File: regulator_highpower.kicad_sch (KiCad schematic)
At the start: 14 parts, among them U12 I3A4W008A033V-001-R, U13 INA180A2

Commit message: improvements with derick
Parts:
- D11: value BLUE -> GREEN
- R43: value Rup -> 8K2
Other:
- note added: "SMPS Regulator (1/32 Brick DC/DC)"
- note added: "Vref = 0.6V Vonom = 2.59V F = 36500 G = 511 Rext = (Vref * F) / (Vout - Vonom) - G Vout = 5.1V -> 8.214K Vout = 18V -> 910"
- note removed: "SMPS Regulator"
- note removed: "TODO: Rup TODO: DAC?"
- moved on the sheet: C27, C28, C29, R43, U12

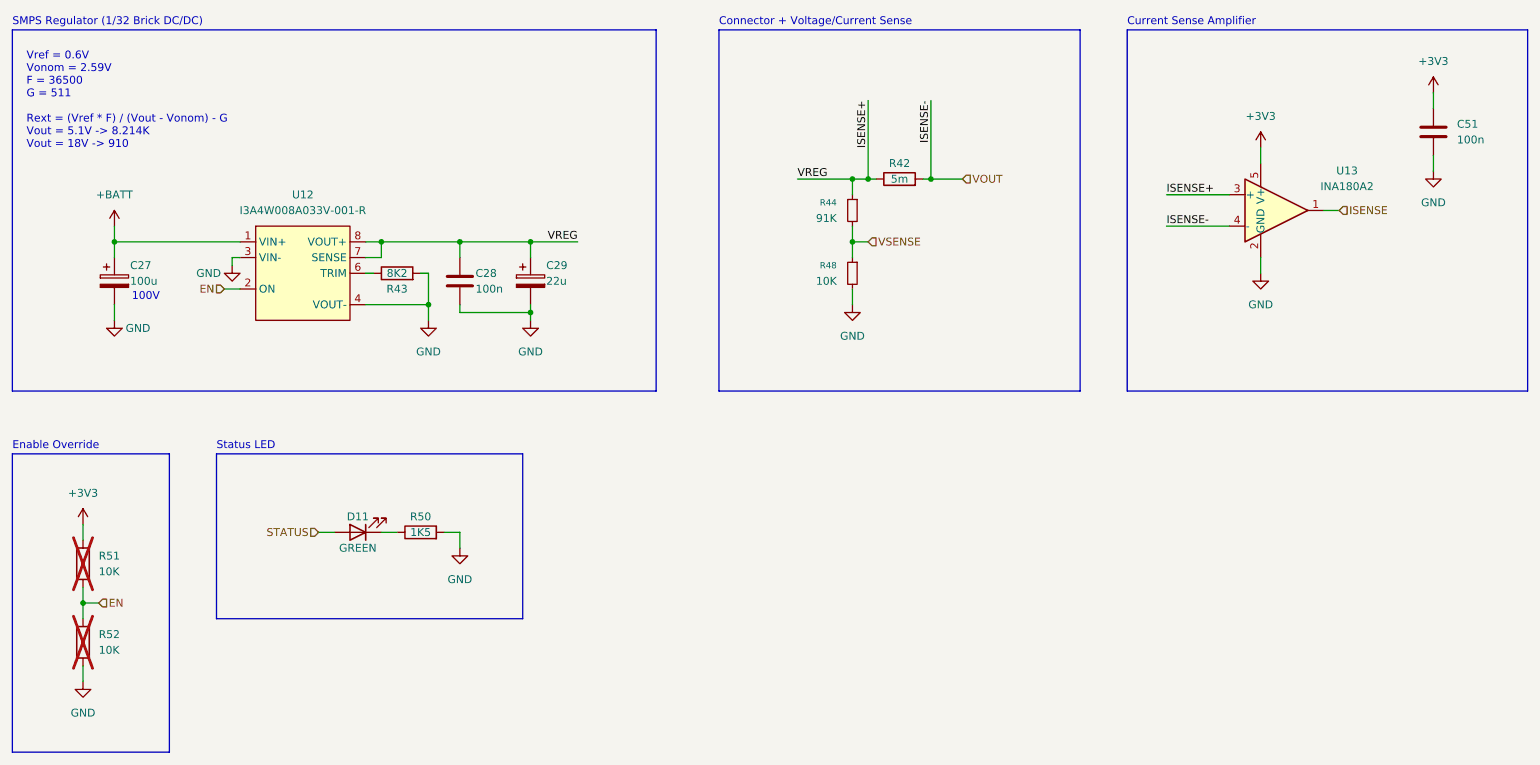
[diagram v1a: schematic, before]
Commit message: updated layout for fault led with new circuit, rerouted
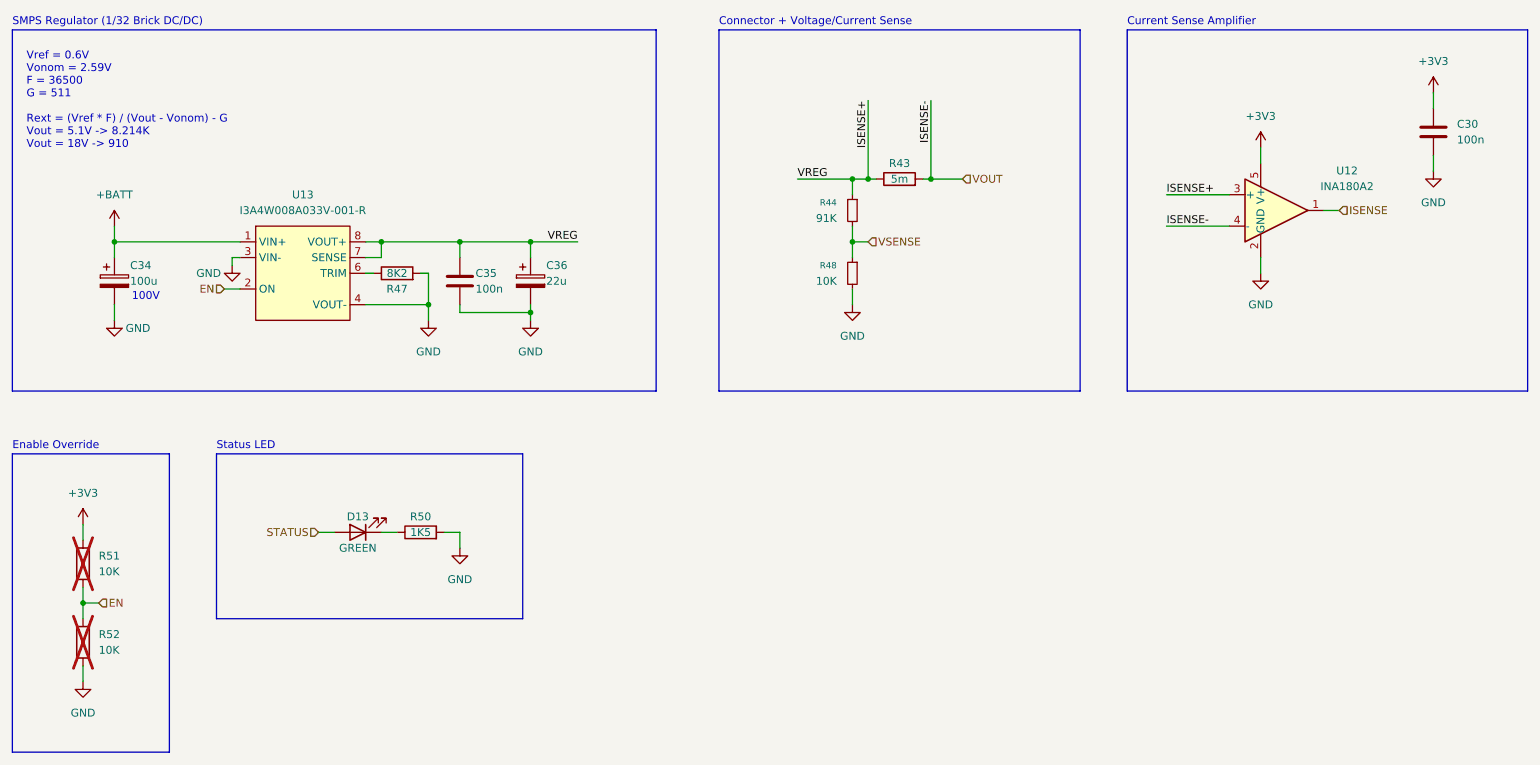
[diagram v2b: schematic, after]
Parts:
- renumbered C51 to C30, C27 to C34, C28 to C35, C29 to C36, D11 to D13, R42 to R43, R43 to R47, U13 to U12, U12 to U13
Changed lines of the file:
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@@
 		(dnp no)
 		(fields_autoplaced yes)
-		(property "Reference" "#PWR071"
+		(property "Reference" "#PWR0101"
 			(at 36.83 57.15 0)
 			(effects
@@
 			(project "vrb"
 				(path "/59a9b615-ea12-4a8c-9228-b32f861e8d75/eb1e4a76-3344-4a3b-8543-2ea356ffbe51"
-					(reference "#PWR071")
+					(reference "#PWR0101")
 					(unit 1)
 				)
@@
 		(dnp no)
 		(fields_autoplaced yes)
-		(property "Reference" "U12"
+		(property "Reference" "U13"
 			(at 67.31 48.26 0)
 			(effects
@@
 			(project "vrb"
 				(path "/59a9b615-ea12-4a8c-9228-b32f861e8d75/eb1e4a76-3344-4a3b-8543-2ea356ffbe51"
-					(reference "U12")
+					(reference "U13")
 					(unit 1)
 				)
@@
 		(on_board yes)
 		(dnp no)
-		(property "Reference" "C28"
+		(property "Reference" "C35"
 			(at 95.25 60.96 0)
 			(effects
@@
 			(project "vrb"
 				(path "/59a9b615-ea12-4a8c-9228-b32f861e8d75/eb1e4a76-3344-4a3b-8543-2ea356ffbe51"
-					(reference "C28")
+					(reference "C35")
 					(unit 1)
 				)
@@
 		(on_board yes)
 		(dnp no)
-		(property "Reference" "R42"
+		(property "Reference" "R43"
 			(at 163.83 43.18 90)
 			(effects
@@
 			(project "vrb"
 				(path "/59a9b615-ea12-4a8c-9228-b32f861e8d75/eb1e4a76-3344-4a3b-8543-2ea356ffbe51"
-					(reference "R42")
+					(reference "R43")
 					(unit 1)
 				)
@@
 		(dnp no)
 		(fields_autoplaced yes)
-		(property "Reference" "#PWR072"
+		(property "Reference" "#PWR092"
 			(at 222.25 44.45 0)
 			(effects
@@
 			(project "vrb"
 				(path "/59a9b615-ea12-4a8c-9228-b32f861e8d75/eb1e4a76-3344-4a3b-8543-2ea356ffbe51"
-					(reference "#PWR072")
+					(reference "#PWR092")
 					(unit 1)
 				)
@@
 		(dnp no)
 		(fields_autoplaced yes)
-		(property "Reference" "U13"
+		(property "Reference" "U12"
 			(at 236.22 44.3798 0)
 			(effects
@@
 			(project ""
 				(path "/59a9b615-ea12-4a8c-9228-b32f861e8d75/eb1e4a76-3344-4a3b-8543-2ea356ffbe51"
-					(reference "U13")
+					(reference "U12")
 					(unit 1)
 				)
@@
 		(on_board yes)
 		(dnp no)
-		(property "Reference" "#PWR083"
+		(property "Reference" "#PWR0109"
 			(at 36.83 74.93 0)
 			(effects
@@
 			(project "vrb"
 				(path "/59a9b615-ea12-4a8c-9228-b32f861e8d75/eb1e4a76-3344-4a3b-8543-2ea356ffbe51"
-					(reference "#PWR083")
+					(reference "#PWR0109")
 					(unit 1)
 				)
@@
 		(on_board yes)
 		(dnp no)
-		(property "Reference" "D11"
+		(property "Reference" "D13"
 			(at 76.2 100.33 0)
 			(effects
@@
 			(project "vrb"
 				(path "/59a9b615-ea12-4a8c-9228-b32f861e8d75/eb1e4a76-3344-4a3b-8543-2ea356ffbe51"
-					(reference "D11")
+					(reference "D13")
 					(unit 1)
 				)
@@
 		(dnp no)
 		(fields_autoplaced yes)
-		(property "Reference" "#PWR0177"
+		(property "Reference" "#PWR098"
 			(at 250.19 50.8 0)
 			(effects
@@
 			(project "vrb"
 				(path "/59a9b615-ea12-4a8c-9228-b32f861e8d75/eb1e4a76-3344-4a3b-8543-2ea356ffbe51"
-					(reference "#PWR0177")
+					(reference "#PWR098")
 					(unit 1)
 				)
@@
 		(dnp no)
 		(fields_autoplaced yes)
-		(property "Reference" "C51"
+		(property "Reference" "C30"
 			(at 254 36.8299 0)
 			(effects
@@
 			(project "vrb"
 				(path "/59a9b615-ea12-4a8c-9228-b32f861e8d75/eb1e4a76-3344-4a3b-8543-2ea356ffbe51"
-					(reference "C51")
+					(reference "C30")
 					(unit 1)
 				)
@@
 		(dnp no)
 		(fields_autoplaced yes)
-		(property "Reference" "#PWR089"
+		(property "Reference" "#PWR0108"
 			(at 156.21 72.39 0)
 			(effects
@@
 			(project "vrb"
 				(path "/59a9b615-ea12-4a8c-9228-b32f861e8d75/eb1e4a76-3344-4a3b-8543-2ea356ffbe51"
-					(reference "#PWR089")
+					(reference "#PWR0108")
 					(unit 1)
 				)
@@
 		(dnp no)
 		(fields_autoplaced yes)
-		(property "Reference" "#PWR092"
+		(property "Reference" "#PWR0115"
 			(at 92.71 111.76 0)
 			(effects
@@
 			(project "vrb"
 				(path "/59a9b615-ea12-4a8c-9228-b32f861e8d75/eb1e4a76-3344-4a3b-8543-2ea356ffbe51"
-					(reference "#PWR092")
+					(reference "#PWR0115")
 					(unit 1)
 				)
@@
 		(dnp no)
 		(fields_autoplaced yes)
-		(property "Reference" "#PWR093"
+		(property "Reference" "#PWR0116"
 			(at 31.75 133.35 0)
 			(effects
@@
 			(project "vrb"
 				(path "/59a9b615-ea12-4a8c-9228-b32f861e8d75/eb1e4a76-3344-4a3b-8543-2ea356ffbe51"
-					(reference "#PWR093")
+					(reference "#PWR0116")
 					(unit 1)
 				)
@@
 		(on_board yes)
 		(dnp no)
-		(property "Reference" "#PWR077"
+		(property "Reference" "#PWR0105"
 			(at 55.88 66.04 0)
 			(effects
@@
 			(project "vrb"
 				(path "/59a9b615-ea12-4a8c-9228-b32f861e8d75/eb1e4a76-3344-4a3b-8543-2ea356ffbe51"
-					(reference "#PWR077")
+					(reference "#PWR0105")
 					(unit 1)
 				)
@@
 		(dnp no)
 		(fields_autoplaced yes)
-		(property "Reference" "#PWR084"
+		(property "Reference" "#PWR0111"
 			(at 104.14 74.93 0)
 			(effects
@@
 			(project "vrb"
 				(path "/59a9b615-ea12-4a8c-9228-b32f861e8d75/eb1e4a76-3344-4a3b-8543-2ea356ffbe51"
-					(reference "#PWR084")
+					(reference "#PWR0111")
 					(unit 1)
 				)
@@
 		(on_board yes)
 		(dnp no)
-		(property "Reference" "C27"
+		(property "Reference" "C34"
 			(at 39.37 59.69 0)
 			(effects
@@
 			(project "vrb"
 				(path "/59a9b615-ea12-4a8c-9228-b32f861e8d75/eb1e4a76-3344-4a3b-8543-2ea356ffbe51"
-					(reference "C27")
+					(reference "C34")
 					(unit 1)
 				)
@@
 		(on_board yes)
 		(dnp no)
-		(property "Reference" "R43"
+		(property "Reference" "R47"
 			(at 82.55 63.5 90)
 			(effects
@@
 			(project "vrb"
 				(path "/59a9b615-ea12-4a8c-9228-b32f861e8d75/eb1e4a76-3344-4a3b-8543-2ea356ffbe51"
-					(reference "R43")
+					(reference "R47")
 					(unit 1)
 				)
@@
 		(on_board yes)
 		(dnp no)
-		(property "Reference" "C29"
+		(property "Reference" "C36"
 			(at 106.68 59.69 0)
 			(effects
@@
 			(project "vrb"
 				(path "/59a9b615-ea12-4a8c-9228-b32f861e8d75/eb1e4a76-3344-4a3b-8543-2ea356ffbe51"
-					(reference "C29")
+					(reference "C36")
 					(unit 1)
 				)
@@
 		(dnp no)
 		(fields_autoplaced yes)
-		(property "Reference" "#PWR087"
+		(property "Reference" "#PWR0106"
 			(at 222.25 67.31 0)
 			(effects
@@
 			(project "vrb"
 				(path "/59a9b615-ea12-4a8c-9228-b32f861e8d75/eb1e4a76-3344-4a3b-8543-2ea356ffbe51"
-					(reference "#PWR087")
+					(reference "#PWR0106")
 					(unit 1)
 				)
@@
 		(dnp no)
 		(fields_autoplaced yes)
-		(property "Reference" "#PWR0182"
+		(property "Reference" "#PWR0110"
 			(at 87.63 74.93 0)
 			(effects
@@
 			(project ""
 				(path "/59a9b615-ea12-4a8c-9228-b32f861e8d75/eb1e4a76-3344-4a3b-8543-2ea356ffbe51"
-					(reference "#PWR0182")
+					(reference "#PWR0110")
 					(unit 1)
 				)
@@
 		(dnp no)
 		(fields_autoplaced yes)
-		(property "Reference" "#PWR091"
+		(property "Reference" "#PWR0114"
 			(at 31.75 105.41 0)
 			(effects
@@
 			(project "vrb"
 				(path "/59a9b615-ea12-4a8c-9228-b32f861e8d75/eb1e4a76-3344-4a3b-8543-2ea356ffbe51"
-					(reference "#PWR091")
+					(reference "#PWR0114")
 					(unit 1)
 				)
@@
 		(dnp no)
 		(fields_autoplaced yes)
-		(property "Reference" "#PWR0176"
+		(property "Reference" "#PWR087"
 			(at 250.19 35.56 0)
 			(effects
@@
 			(project "vrb"
 				(path "/59a9b615-ea12-4a8c-9228-b32f861e8d75/eb1e4a76-3344-4a3b-8543-2ea356ffbe51"
-					(reference "#PWR0176")
-					(unit 1)
-				)
+					(reference "#PWR087")
+					(unit 1)
+				)
